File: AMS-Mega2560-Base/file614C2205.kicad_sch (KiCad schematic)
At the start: 5 parts, among them IC1 CD74HC4050ME4, IC2 CD74HC4050ME4, J6 Conn_01x03, J7 Conn_01x08

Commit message: fixing some library settings and updating some schematics
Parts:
- R1: footprint Resistor_THT:R_Axial_DIN0207_L6.3mm_D2.5mm_P5.08mm_Vertical -> Resistor_THT:R_Axial_DIN0207_L6.3mm_D2.5mm_P2.54mm_Vertical
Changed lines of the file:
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@@
       (effects (font (size 1.27 1.27)) (justify left))
     )
-    (property "Footprint" "Resistor_THT:R_Axial_DIN0207_L6.3mm_D2.5mm_P5.08mm_Vertical" (id 2) (at 187.452 71.12 90)
+    (property "Footprint" "Resistor_THT:R_Axial_DIN0207_L6.3mm_D2.5mm_P2.54mm_Vertical" (id 2) (at 187.452 71.12 90)
       (effects (font (size 1.27 1.27)) hide)
     )

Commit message: BaseBoard fixes and updates. doing schematic work.
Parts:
- added J8: AdafruitUltimateGPS, Connector_PinSocket_2.54mm:PinSocket_1x09_P2.54mm_Vertical, symbol Connector_Generic:Conn_01x09
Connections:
- net +5VP: now also J8.8 (Pin_8)
- net GND: now also J8.7 (Pin_7)
- new net 3.3: J8.1 (Pin_1)
- new net EN: J8.2 (Pin_2)
- new net FIX: J8.4 (Pin_4)
- new net GPSBat: J8.3 (Pin_3)
- new net GPSRX: J8.6 (Pin_6)
- new net GPSTX: J8.5 (Pin_5)
- new net PPS: J8.9 (Pin_9)
- no-connect marks 7 -> 11
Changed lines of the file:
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@@
   (no_connect (at 205.74 59.69))
   (no_connect (at 81.28 45.72))
+  (no_connect (at 247.65 105.41))
   (no_connect (at 81.28 118.11))
+  (no_connect (at 227.33 105.41))
   (no_connect (at 81.28 110.49))
   (no_connect (at 81.28 38.1))
+  (no_connect (at 234.95 105.41))
+  (no_connect (at 229.87 105.41))
   (wire (pts (xy 49.53 107.95) (xy 53.34 107.95))
     (stroke (width 0) (type default) (color 0 0 0 0))
   )
+  (wire (pts (xy 227.33 105.41) (xy 227.33 100.33))
+    (stroke (width 0) (type default) (color 0 0 0 0))
+  )
   (wire (pts (xy 200.66 62.23) (xy 205.74 62.23))
     (stroke (width 0) (type default) (color 0 0 0 0))
@@
     (stroke (width 0) (type default) (color 0 0 0 0))
   )
+  (wire (pts (xy 237.49 100.33) (xy 237.49 114.3))
+    (stroke (width 0) (type default) (color 0 0 0 0))
+  )
   (wire (pts (xy 86.36 113.03) (xy 81.28 113.03))
     (stroke (width 0) (type default) (color 0 0 0 0))
@@
     (stroke (width 0) (type default) (color 0 0 0 0))
   )
+  (wire (pts (xy 232.41 100.33) (xy 232.41 114.3))
+    (stroke (width 0) (type default) (color 0 0 0 0))
+  )
   (wire (pts (xy 53.34 40.64) (xy 50.8 40.64))
     (stroke (width 0) (type default) (color 0 0 0 0))
@@
     (stroke (width 0) (type default) (color 0 0 0 0))
   )
+  (wire (pts (xy 247.65 105.41) (xy 247.65 100.33))
+    (stroke (width 0) (type default) (color 0 0 0 0))
+  )
   (wire (pts (xy 205.74 57.15) (xy 204.47 57.15))
     (stroke (width 0) (type default) (color 0 0 0 0))
@@
     (stroke (width 0) (type default) (color 0 0 0 0))
   )
+  (wire (pts (xy 240.03 100.33) (xy 240.03 114.3))
+    (stroke (width 0) (type default) (color 0 0 0 0))
+  )
   (wire (pts (xy 53.34 102.87) (xy 53.34 97.79))
     (stroke (width 0) (type default) (color 0 0 0 0))
   )
+  (wire (pts (xy 242.57 107.95) (xy 242.57 100.33))
+    (stroke (width 0) (type default) (color 0 0 0 0))
+  )
+  (wire (pts (xy 245.11 107.95) (xy 245.11 100.33))
+    (stroke (width 0) (type default) (color 0 0 0 0))
+  )
   (wire (pts (xy 50.8 48.26) (xy 53.34 48.26))
     (stroke (width 0) (type default) (color 0 0 0 0))
@@
     (stroke (width 0) (type default) (color 0 0 0 0))
   )
+  (wire (pts (xy 229.87 105.41) (xy 229.87 100.33))
+    (stroke (width 0) (type default) (color 0 0 0 0))
+  )
   (wire (pts (xy 85.09 50.8) (xy 81.28 50.8))
     (stroke (width 0) (type default) (color 0 0 0 0))
   )
+  (wire (pts (xy 234.95 105.41) (xy 234.95 100.33))
+    (stroke (width 0) (type default) (color 0 0 0 0))
+  )
   (wire (pts (xy 96.52 101.6) (xy 102.87 101.6))
     (stroke (width 0) (type default) (color 0 0 0 0))
+  )
+  (label "GND" (at 242.57 105.41 90)
+    (effects (font (size 1.27 1.27)) (justify left bottom))
+  )
+  (label "VIN" (at 245.11 105.41 90)
+    (effects (font (size 1.27 1.27)) (justify left bottom))
+  )
+  (label "FIX" (at 234.95 105.41 90)
+    (effects (font (size 1.27 1.27)) (justify left bottom))
+  )
+  (label "PPS" (at 247.65 105.41 90)
+    (effects (font (size 1.27 1.27)) (justify left bottom))
+  )
+  (label "Vbat" (at 232.41 105.41 90)
+    (effects (font (size 1.27 1.27)) (justify left bottom))
+  )
+  (label "EN" (at 229.87 105.41 90)
+    (effects (font (size 1.27 1.27)) (justify left bottom))
+  )
+  (label "3.3" (at 227.33 105.41 90)
+    (effects (font (size 1.27 1.27)) (justify left bottom))
+  )
+  (global_label "GPSTX" (shape input) (at 237.49 114.3 270) (fields_autoplaced)
+    (effects (font (size 1.27 1.27)) (justify right))
+    (property "Intersheet References" "${INTERSHEET_REFS}" (id 0) (at 182.88 60.96 0)
+      (effects (font (size 1.27 1.27)) hide)
+    )
+  )
+  (global_label "GPSBat" (shape input) (at 232.41 114.3 270) (fields_autoplaced)
+    (effects (font (size 1.27 1.27)) (justify right))
+    (property "Intersheet References" "${INTERSHEET_REFS}" (id 0) (at 182.88 60.96 0)
+      (effects (font (size 1.27 1.27)) hide)
+    )
+  )
+  (global_label "GPSRX" (shape input) (at 240.03 114.3 270) (fields_autoplaced)
+    (effects (font (size 1.27 1.27)) (justify right))
+    (property "Intersheet References" "${INTERSHEET_REFS}" (id 0) (at 182.88 60.96 0)
+      (effects (font (size 1.27 1.27)) hide)
+    )
   )
   (hierarchical_label "3.3MOSI" (shape input) (at 50.8 45.72 180)
@@
   (symbol (lib_id "power:+3.3V") (at 53.34 33.02 0) (unit 1)
     (in_bom yes) (on_board yes)
-    (property "Reference" "#PWR012" (id 0) (at 53.34 36.83 0)
+    (property "Reference" "#PWR09" (id 0) (at 53.34 36.83 0)
       (effects (font (size 1.27 1.27)) hide)
     )
@@
   (symbol (lib_id "power:GND") (at 53.34 60.96 0) (unit 1)
     (in_bom yes) (on_board yes)
-    (property "Reference" "#PWR013" (id 0) (at 53.34 67.31 0)
+    (property "Reference" "#PWR010" (id 0) (at 53.34 67.31 0)
       (effects (font (size 1.27 1.27)) hide)
     )
@@
   (symbol (lib_id "power:+3.3V") (at 53.34 97.79 0) (unit 1)
     (in_bom yes) (on_board yes)
-    (property "Reference" "#PWR014" (id 0) (at 53.34 101.6 0)
+    (property "Reference" "#PWR011" (id 0) (at 53.34 101.6 0)
       (effects (font (size 1.27 1.27)) hide)
     )
@@
   (symbol (lib_id "power:GND") (at 53.34 125.73 0) (unit 1)
     (in_bom yes) (on_board yes)
-    (property "Reference" "#PWR015" (id 0) (at 53.34 132.08 0)
+    (property "Reference" "#PWR012" (id 0) (at 53.34 132.08 0)
       (effects (font (size 1.27 1.27)) hide)
     )
@@
   (symbol (lib_id "power:GND") (at 200.66 62.23 270) (mirror x) (unit 1)
     (in_bom yes) (on_board yes)
-    (property "Reference" "#PWR018" (id 0) (at 194.31 62.23 0)
+    (property "Reference" "#PWR015" (id 0) (at 194.31 62.23 0)
       (effects (font (size 1.27 1.27)) hide)
     )
@@
   (symbol (lib_id "power:+5VP") (at 204.47 55.88 0) (unit 1)
     (in_bom yes) (on_board yes)
-    (property "Reference" "#PWR019" (id 0) (at 204.47 59.69 0)
+    (property "Reference" "#PWR016" (id 0) (at 204.47 59.69 0)
       (effects (font (size 1.27 1.27)) hide)
     )
@@
   (symbol (lib_id "power:+5VP") (at 189.23 63.5 0) (unit 1)
     (in_bom yes) (on_board yes)
-    (property "Reference" "#PWR017" (id 0) (at 189.23 67.31 0)
+    (property "Reference" "#PWR014" (id 0) (at 189.23 67.31 0)
       (effects (font (size 1.27 1.27)) hide)
     )
@@
   (symbol (lib_id "power:GND") (at 102.87 106.68 0) (unit 1)
     (in_bom yes) (on_board yes)
-    (property "Reference" "#PWR016" (id 0) (at 102.87 113.03 0)
+    (property "Reference" "#PWR013" (id 0) (at 102.87 113.03 0)
       (effects (font (size 1.27 1.27)) hide)
     )
@@
       (effects (font (size 1.27 1.27)) hide)
     )
+    (pin "1")
+  )
+  (symbol (lib_id "Connector_Generic:Conn_01x09") (at 237.49 95.25 90) (unit 1)
+    (in_bom yes) (on_board yes)
+    (property "Reference" "J8" (id 0) (at 237.5916 89.7382 90))
+    (property "Value" "AdafruitUltimateGPS" (id 1) (at 237.5916 92.0496 90))
+    (property "Footprint" "Connector_PinSocket_2.54mm:PinSocket_1x09_P2.54mm_Vertical" (id 2) (at 237.49 95.25 0)
+      (effects (font (size 1.27 1.27)) hide)
+    )
+    (property "Datasheet" "~" (id 3) (at 237.49 95.25 0)
+      (effects (font (size 1.27 1.27)) hide)
+    )
+    (pin "1")
+    (pin "2")
+    (pin "3")
+    (pin "4")
+    (pin "5")
+    (pin "6")
+    (pin "7")
+    (pin "8")
+    (pin "9")
+  )
+  (symbol (lib_id "power:+5VP") (at 245.11 107.95 0) (mirror x) (unit 1)
+    (in_bom yes) (on_board yes)
+    (property "Reference" "#PWR018" (id 0) (at 245.11 104.14 0)
+      (effects (font (size 1.27 1.27)) hide)
+    )
+    (property "Value" "+5VP" (id 1) (at 245.491 112.3442 0))
+    (property "Footprint" "" (id 2) (at 245.11 107.95 0)
+      (effects (font (size 1.27 1.27)) hide)
+    )
+    (property "Datasheet" "" (id 3) (at 245.11 107.95 0)
+      (effects (font (size 1.27 1.27)) hide)
+    )
+    (pin "1")
+  )
+  (symbol (lib_id "power:GND") (at 242.57 107.95 0) (unit 1)
+    (in_bom yes) (on_board yes)
+    (property "Reference" "#PWR017" (id 0) (at 242.57 114.3 0)
+      (effects (font (size 1.27 1.27)) hide)
+    )
+    (property "Value" "GND" (id 1) (at 242.697 112.3442 0))
+    (property "Footprint" "" (id 2) (at 242.57 107.95 0)
+      (effects (font (size 1.27 1.27)) hide)
+    )
+    (property "Datasheet" "" (id 3) (at 242.57 107.95 0)
+      (effects (font (size 1.27 1.27)) hide)
+    )

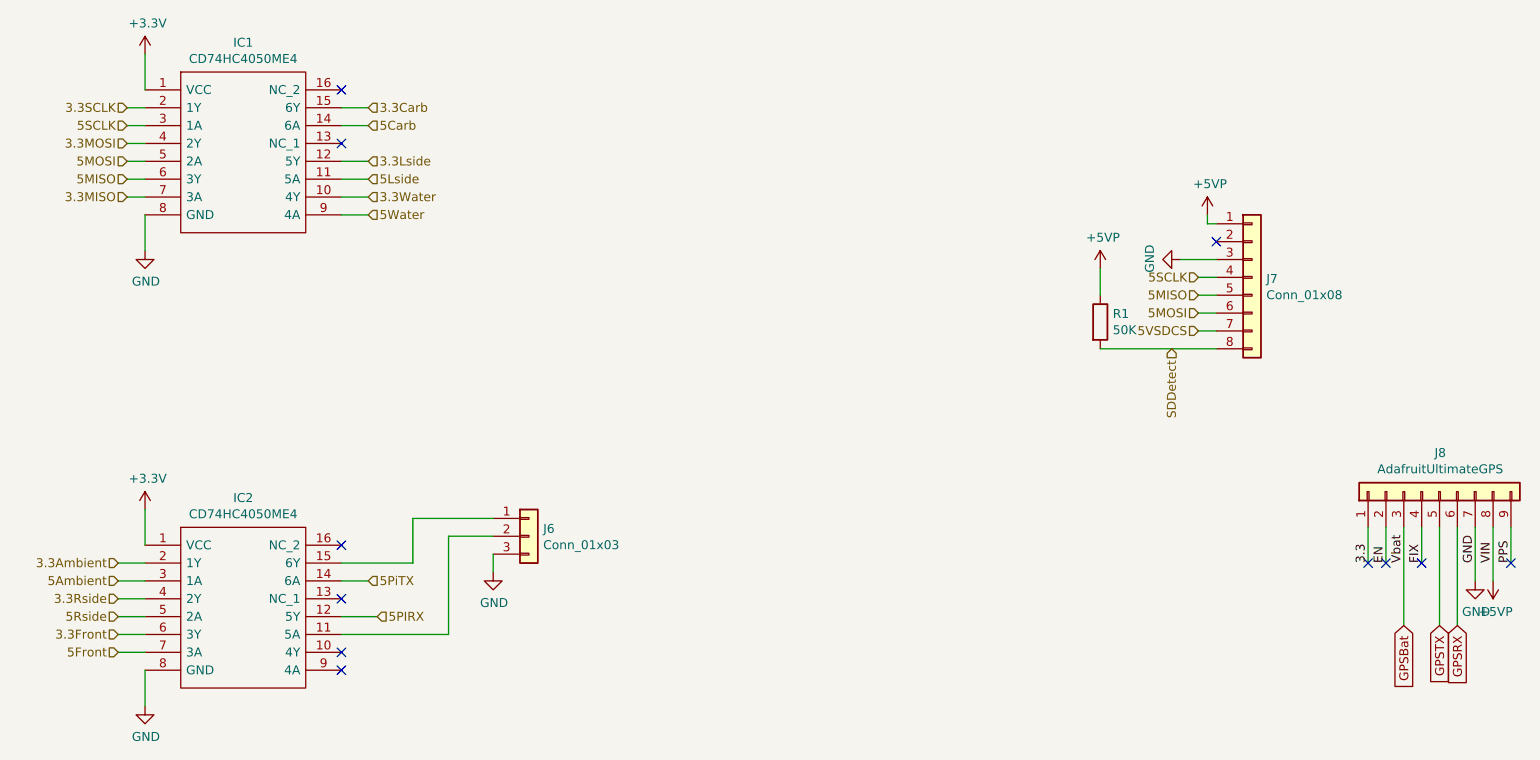
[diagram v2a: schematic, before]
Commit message: trying to fix the PCB layout.
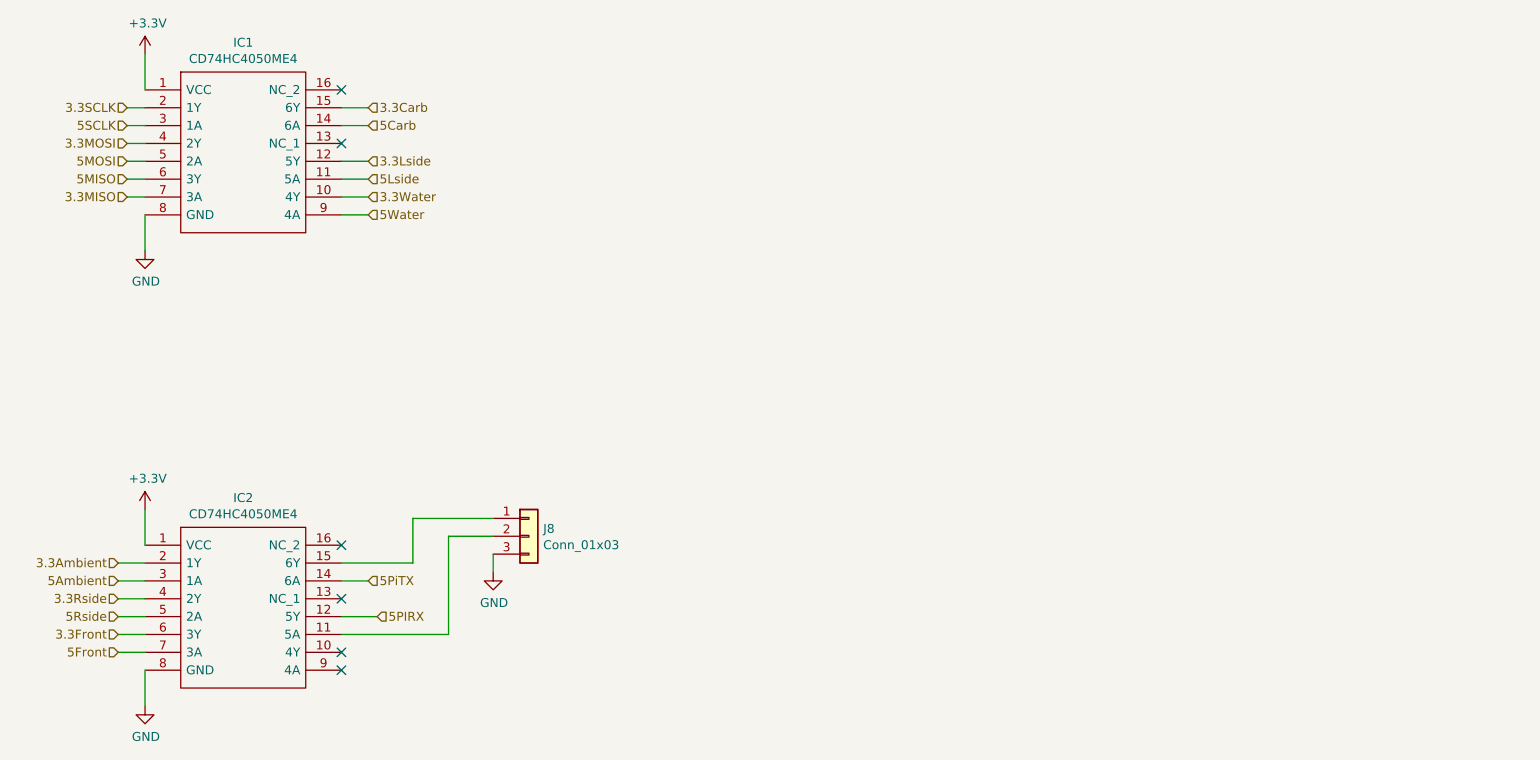
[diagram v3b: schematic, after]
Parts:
- removed J7: Conn_01x08, Connector_PinSocket_2.54mm:PinSocket_1x08_P2.54mm_Horizontal, symbol Connector_Generic:Conn_01x08
- removed J8: AdafruitUltimateGPS, Connector_PinSocket_2.54mm:PinSocket_1x09_P2.54mm_Vertical, symbol Connector_Generic:Conn_01x09
- removed R1: 50K, Resistor_THT:R_Axial_DIN0207_L6.3mm_D2.5mm_P2.54mm_Vertical, symbol Device:R
- renumbered J6 to J8
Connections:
- no-connect marks 11 -> 6

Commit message: rollback and file clean up.
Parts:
- added J7: Conn_01x08, Connector_PinSocket_2.54mm:PinSocket_1x08_P2.54mm_Horizontal, symbol Connector_Generic:Conn_01x08
- added J8: AdafruitUltimateGPS, Connector_PinSocket_2.54mm:PinSocket_1x09_P2.54mm_Vertical, symbol Connector_Generic:Conn_01x09
- added R1: 50K, Resistor_THT:R_Axial_DIN0207_L6.3mm_D2.5mm_P2.54mm_Vertical, symbol Device:R
- renumbered J8 to J6
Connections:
- net 5MISO: now also J7.5 (Pin_5)
- net 5MOSI: now also J7.6 (Pin_6)
- net 5SCLK: now also J7.4 (Pin_4)
- net GND: now also J7.3 (Pin_3), J8.7 (Pin_7)
- new net +5VP: J7.1 (Pin_1), J8.8 (Pin_8), R1.1
- new net 3.3: J8.1 (Pin_1)
- new net 5VSDCS: J7.7 (Pin_7)
- new net EN: J8.2 (Pin_2)
- new net FIX: J8.4 (Pin_4)
- new net GPSBat: J8.3 (Pin_3)
- new net GPSRX: J8.6 (Pin_6)
- new net GPSTX: J8.5 (Pin_5)
- new net PPS: J8.9 (Pin_9)
- new net SDDetect: J7.8 (Pin_8), R1.2
- no-connect marks 6 -> 11

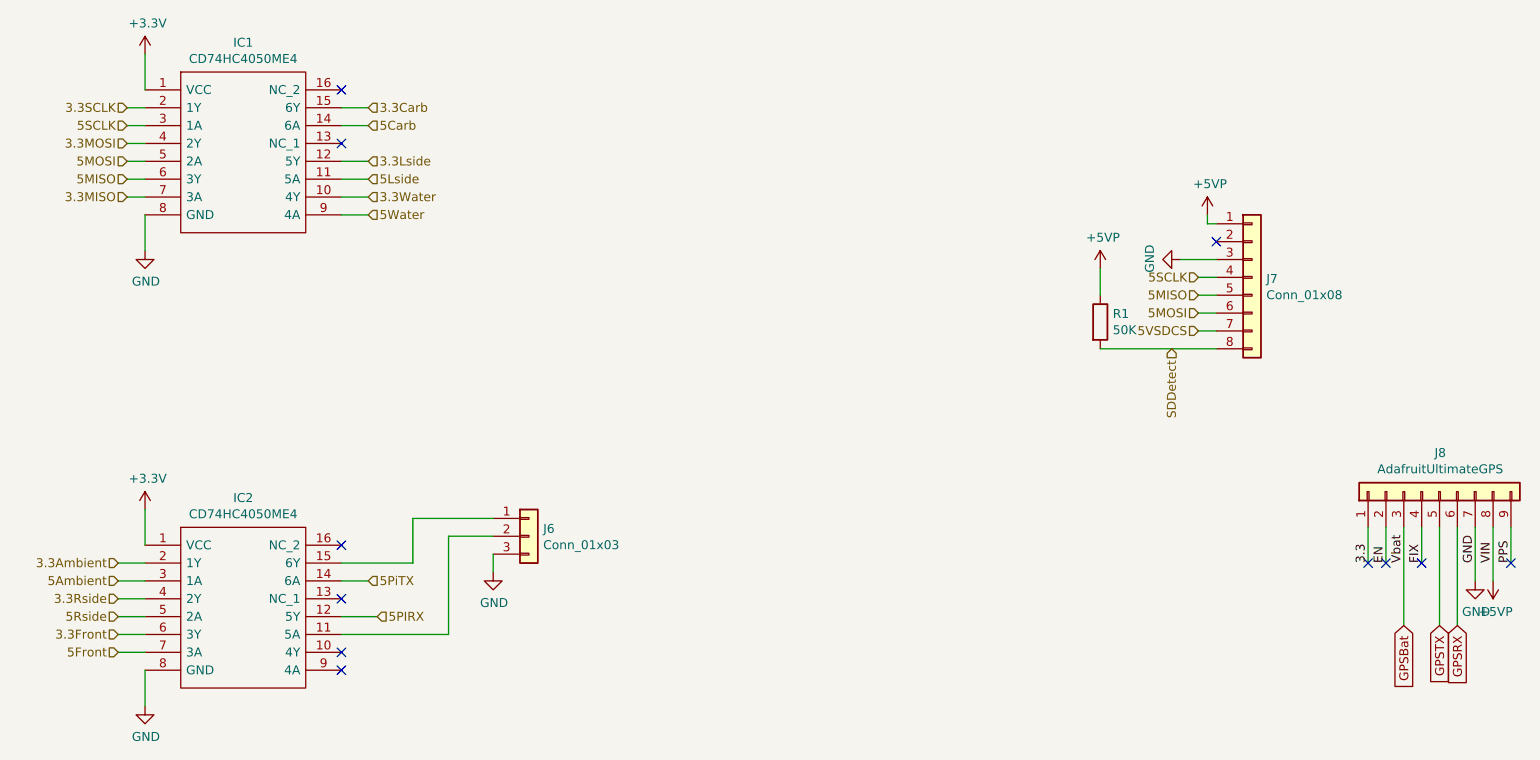
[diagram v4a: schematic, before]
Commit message: fixed the messed up references and cleaned up the schematic.
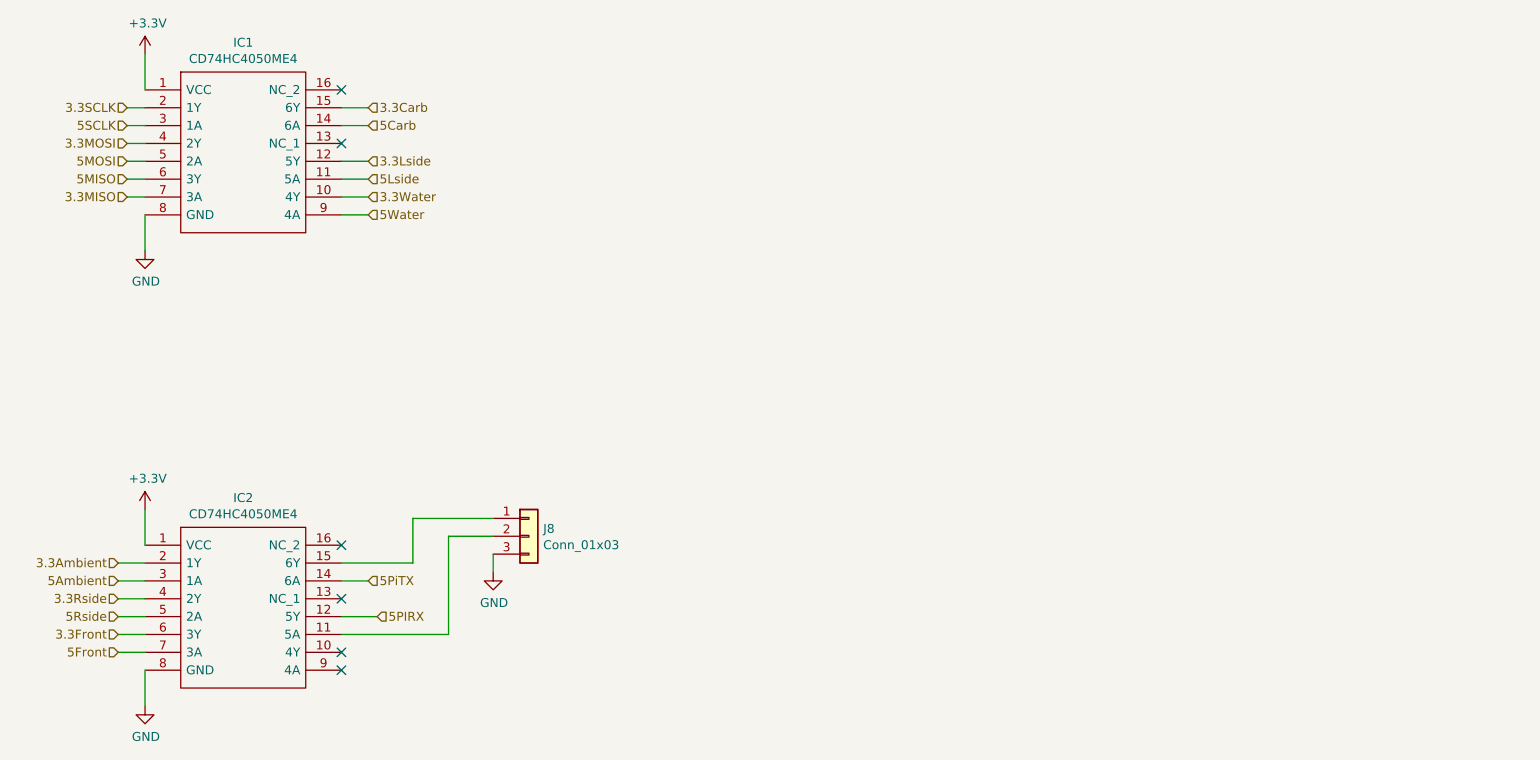
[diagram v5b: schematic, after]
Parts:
- removed J7: Conn_01x08, Connector_PinSocket_2.54mm:PinSocket_1x08_P2.54mm_Horizontal, symbol Connector_Generic:Conn_01x08
- removed J8: AdafruitUltimateGPS, Connector_PinSocket_2.54mm:PinSocket_1x09_P2.54mm_Vertical, symbol Connector_Generic:Conn_01x09
- removed R1: 50K, Resistor_THT:R_Axial_DIN0207_L6.3mm_D2.5mm_P2.54mm_Vertical, symbol Device:R
- renumbered J6 to J8
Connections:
- no-connect marks 11 -> 6
